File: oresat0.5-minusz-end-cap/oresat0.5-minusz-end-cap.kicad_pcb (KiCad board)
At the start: 2 copper layers, 106 x 106 mm, 36 parts, among them U1 TCA9543A-PW, U3 HMC5883L, U4 HMC5883L

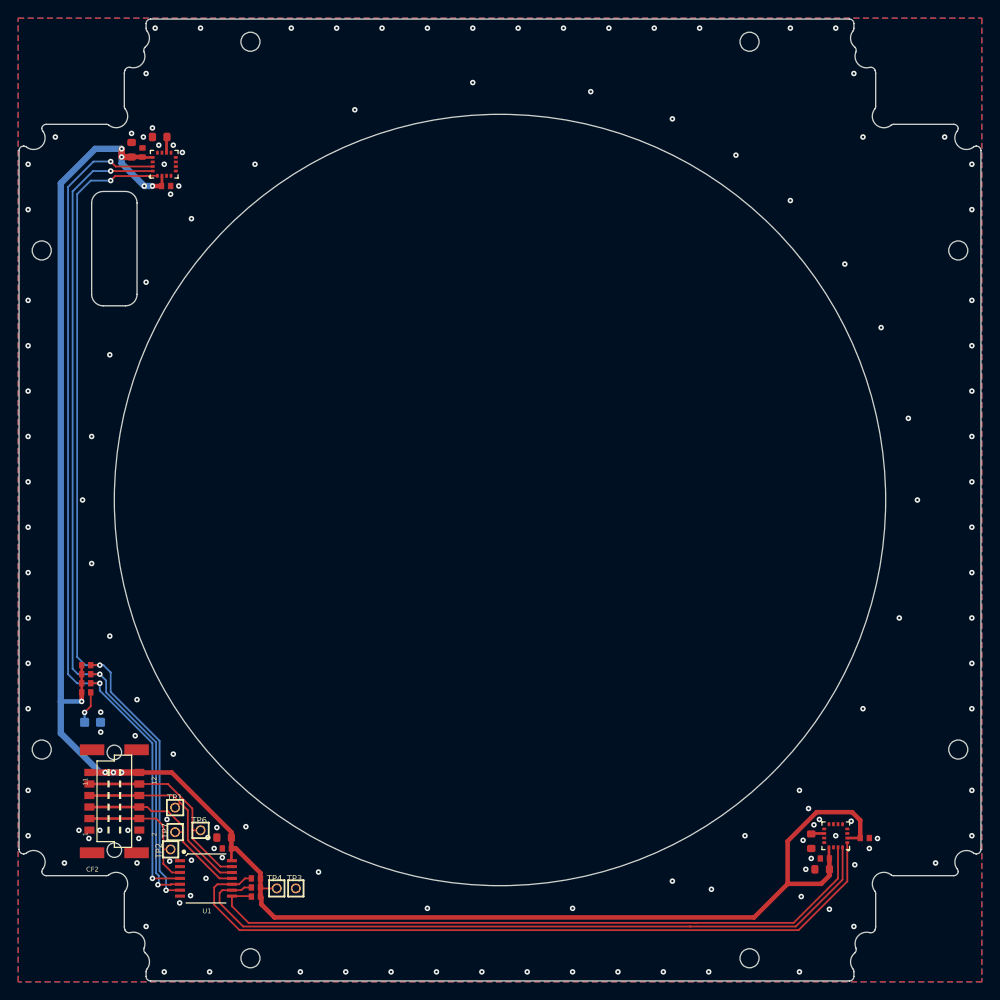
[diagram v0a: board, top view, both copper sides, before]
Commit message: Updated both oresat0.5 end caps. Fixed layout, and added patch antennas
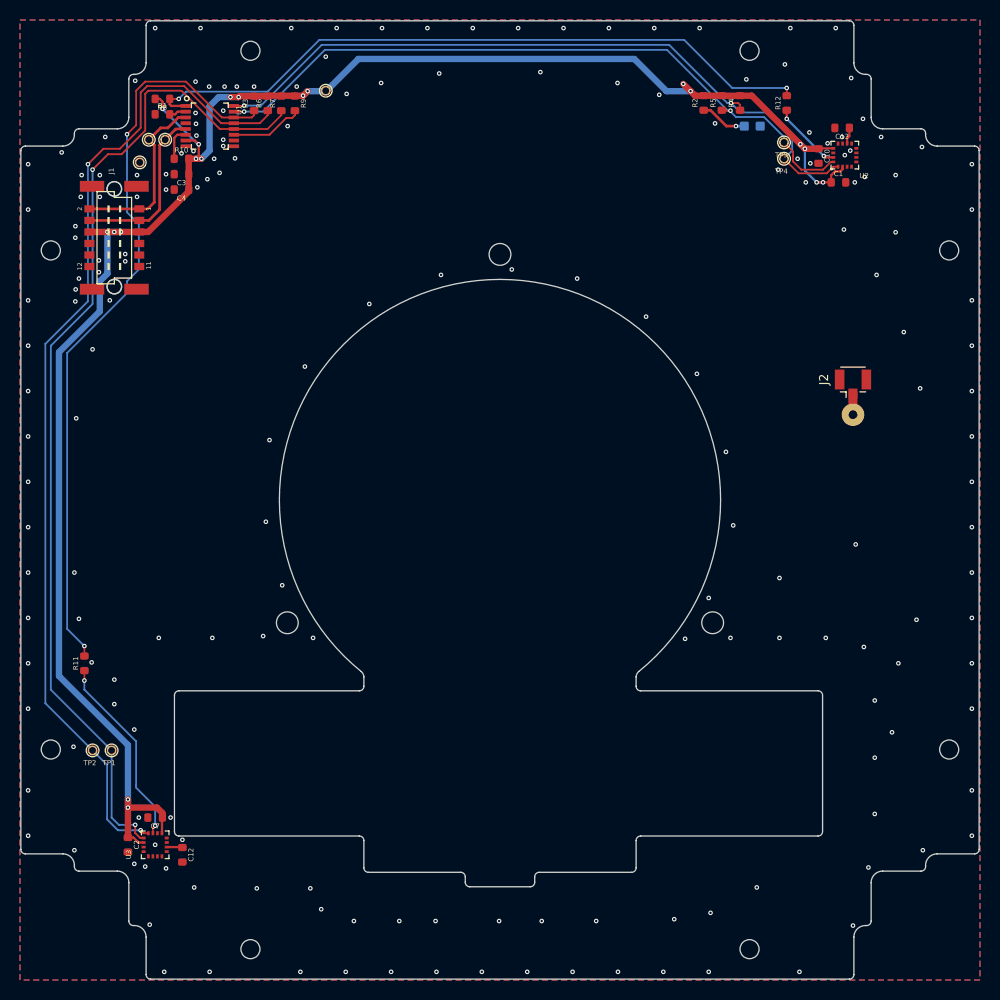
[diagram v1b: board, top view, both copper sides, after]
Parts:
- removed @HOLE0, @HOLE1, @HOLE2, @HOLE3, @HOLE4, @HOLE5, @HOLE6, @HOLE7: , 
- removed C15, C19: 4.7u, minusz-end-cap:.0603-B-NOSILK
- removed CF2: J-HARWIN-M55-70X1242R, minusz-end-cap:HARWIN-M55-70X1242R
- removed U4: HMC5883L, minusz-end-cap:QLGA-16(3X3)
- added ANT1: GP.1575.25.2.A.02, oresat-misc:Taoglas-GPS-Patch-Antenna, B.Cu at (187.4, 93.1)
- added J1: , oresat0.5-minusz-end-cap:HARWIN-M55-70X1242R, F.Cu at (106.0, 76.1)
- added J2: U.FL-R-SMA, Connector_Coaxial:U.FL_Hirose_U.FL-R-SMT-1_Vertical, F.Cu at (187.4, 92.2)
- added R10: , oresat0.5-minusz-end-cap:.0603-B-NOSILK, F.Cu at (113.4, 67.4)
- added R11: NP, oresat0.5-minusz-end-cap:.0603-B-NOSILK, F.Cu at (102.7, 123.0)
- added R12: NP, oresat0.5-minusz-end-cap:.0603-B-NOSILK, F.Cu at (180.1, 61.2)
- added R8: , oresat0.5-minusz-end-cap:.0603-B-NOSILK, F.Cu at (111.3, 60.8)
- added R9: , oresat0.5-minusz-end-cap:.0603-B-NOSILK, F.Cu at (125.9, 61.3)
- added REF**: MountingHole_2.1mm, MountingHole:MountingHole_2.1mm, B.Cu at (198.0, 132.5)
- added REF**: MountingHole_2.1mm, MountingHole:MountingHole_2.1mm, B.Cu at (99.0, 77.5)
- added REF**: MountingHole_2.1mm, MountingHole:MountingHole_2.1mm, B.Cu at (121.0, 154.5)
- added REF**: MountingHole_2.1mm, MountingHole:MountingHole_2.1mm, B.Cu at (198.0, 77.5)
- added REF**: MountingHole_2.1mm, MountingHole:MountingHole_2.1mm, B.Cu at (176.0, 55.5)
- added REF**: MountingHole_2.1mm, MountingHole:MountingHole_2.1mm, B.Cu at (99.0, 132.5)
- added REF**: MountingHole_2.1mm, MountingHole:MountingHole_2.1mm, B.Cu at (176.0, 154.5)
- added REF**: MountingHole_2.1mm, MountingHole:MountingHole_2.1mm, B.Cu at (121.0, 55.5)
- added TP5: TEST-POINT-LARGE-SQUARE, oresat0.5-minusz-end-cap:1X01, B.Cu at (179.8, 65.6)
- added TP8: TEST-POINT-LARGE-SQUARE, oresat0.5-minusz-end-cap:1X01, F.Cu at (108.8, 67.8)
- added U2: , oresat0.5-minusz-end-cap:LGA-16(3X3), F.Cu at (186.5, 67.0)
- C1, C10, C2, C3, C7: value 100n -> (none); footprint minusz-end-cap:.0402-B-NOSILK -> oresat0.5-minusz-end-cap:.0603-B-NOSILK
- C12, C13, C4: value 10u -> (none); footprint minusz-end-cap:.0603-B-NOSILK -> oresat0.5-minusz-end-cap:.0603-B-NOSILK
- D2: value GREEN -> (none); footprint minusz-end-cap:LED-0603 -> oresat0.5-minusz-end-cap:LED-0603
- R1, R3, R4, R5, R6, R7: value 4.7k -> (none); footprint minusz-end-cap:.0402-B-NOSILK -> oresat0.5-minusz-end-cap:.0603-B-NOSILK
- R2: value 2.7k -> (none); footprint minusz-end-cap:.0402-B-NOSILK -> oresat0.5-minusz-end-cap:.0603-B-NOSILK
- TP1, TP2, TP4: value TEST-POINT -> TEST-POINT-LARGE-SQUARE; footprint minusz-end-cap:2MM-TEST-POINT -> oresat0.5-minusz-end-cap:1X01; moved to B.Cu
- TP3, TP6, TP7: value TEST-POINT -> TEST-POINT-LARGE-SQUARE; footprint minusz-end-cap:2MM-TEST-POINT -> oresat0.5-minusz-end-cap:1X01
- U1: value TCA9543A-PW -> (none); footprint minusz-end-cap:TSSOP14-0.65-5.4X4.4MM -> oresat0.5-minusz-end-cap:16-SSOP
- U3: value HMC5883L -> (none); footprint minusz-end-cap:QLGA-16(3X3) -> oresat0.5-minusz-end-cap:LGA-16(3X3)
- moved D2 98.0 mm to (176.3, 63.8)
- moved TP4 97.9 mm to (179.8, 67.4), turned to 180 degrees
- moved R4 95.0 mm to (174.9, 61.2), turned to 90 degrees
- moved R5 94.2 mm to (172.9, 61.2), turned to 90 degrees
- moved R2 94.1 mm to (170.9, 61.2), turned to 90 degrees
- moved R3 87.4 mm to (121.4, 61.3), turned to 90 degrees
- moved R6 86.4 mm to (122.9, 61.3), turned to 90 degrees
- moved R7 85.4 mm to (124.4, 61.3), turned to 90 degrees
- moved TP3 83.8 mm to (111.6, 65.3), turned to -90 degrees
- moved TP7 83.4 mm to (129.3, 59.9), turned to -90 degrees
- moved U1 82.9 mm to (116.5, 63.8)
- moved C2 81.2 mm to (107.5, 143.0), turned to -90 degrees
- moved TP6 76.3 mm to (109.8, 65.3)
- moved C13 75.2 mm to (186.2, 64.0)
- moved U3 75.0 mm to (110.5, 143.0), turned to 90 degrees
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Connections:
- R1 pad 1: ~{INT0} -> GND
- R1 pad 2: 3.3V -> Net-(R1-Pad2)
- R3 pad 1: ~{INT1} -> Net-(R3-Pad1)
- R4 pad 1: SCL0 -> /SCL2
- R5 pad 1: SDA0 -> /SDA2
- R6 pad 1: SD1 -> /SDA1
- R7 pad 1: SC1 -> /SCL1
- TP1 pad 1: I2C-SCL -> /SCL1
- TP2 pad 1: ~{I2C-RESET} -> /SDA1
- TP3 pad 1: GND -> /I2C-SCL
- TP4 pad 1: 3.3V -> /SCL2
- TP6 pad 1: I2C-SDA -> /I2C-SDA
- TP7 pad 1: I2C-~{INT} -> 3.3V
- U1 pad 1: GND -> Net-(R8-Pad1)
- U1 pad 10: SC1 -> GND
- U1 pad 11: I2C-~{INT} -> Net-(R9-Pad2)
- U1 pad 12: I2C-SCL -> /SCL1
- U1 pad 13: I2C-SDA -> /SDA1
- U1 pad 14: 3.3V -> Net-(R3-Pad1)
- U1 pad 2: GND -> Net-(R1-Pad2)
- U1 pad 3: ~{I2C-RESET} -> /I2C-SDA
- U1 pad 4: ~{INT0} -> GND
- U1 pad 5: SDA0 -> /I2C-SCL
- U1 pad 6: SCL0 -> Net-(R10-Pad1)
- U1 pad 7: GND -> 3.3V
- U1 pad 8: ~{INT1} -> GND
- U1 pad 9: SD1 -> GND
- U3 pad 1: SC1 -> /SCL1
- U3 pad 15: ~{INT1} -> Net-(R11-Pad1)
- U3 pad 16: SD1 -> /SDA1
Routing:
- net /SCL1: track 0.00 -> 110.8 mm, vias 0 -> 2
- net /SDA1: track 0.00 -> 110.4 mm, vias 0 -> 2
- net ~{INT0}: track 96.3 -> 0.00 mm, vias 3 -> 0
- net SDA0: track 95.0 -> 0.00 mm, vias 3 -> 0
- net SCL0: track 94.2 -> 0.00 mm, vias 3 -> 0
- net SC1: track 83.9 -> 0.00 mm
- net Net-(R3-Pad1): track 0.00 -> 83.0 mm, vias 0 -> 2
- net SD1: track 80.3 -> 0.00 mm
- net /SCL2: track 0.00 -> 79.8 mm, vias 0 -> 2
- net /SDA2: track 0.00 -> 76.7 mm, vias 0 -> 3
- net ~{INT1}: track 76.3 -> 0.00 mm
- net Net-(R8-Pad1): track 0.00 -> 76.2 mm, vias 0 -> 2
- net I2C-SDA: track 22.3 -> 0.00 mm
- net I2C-SCL: track 21.9 -> 0.00 mm
- net Net-(R11-Pad1): track 0.00 -> 21.3 mm, vias 0 -> 2
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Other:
- board size 106 x 106 mm -> 105.6 x 105.6 mm
- board text added: "2022/02/17"
- board text added: "OreSat0.5 -Z End Cap v1.0"
- board text removed: "OreSat -Z End Cap v1.0"

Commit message: Updated both OreSat0.5 end caps and cleaned up errors
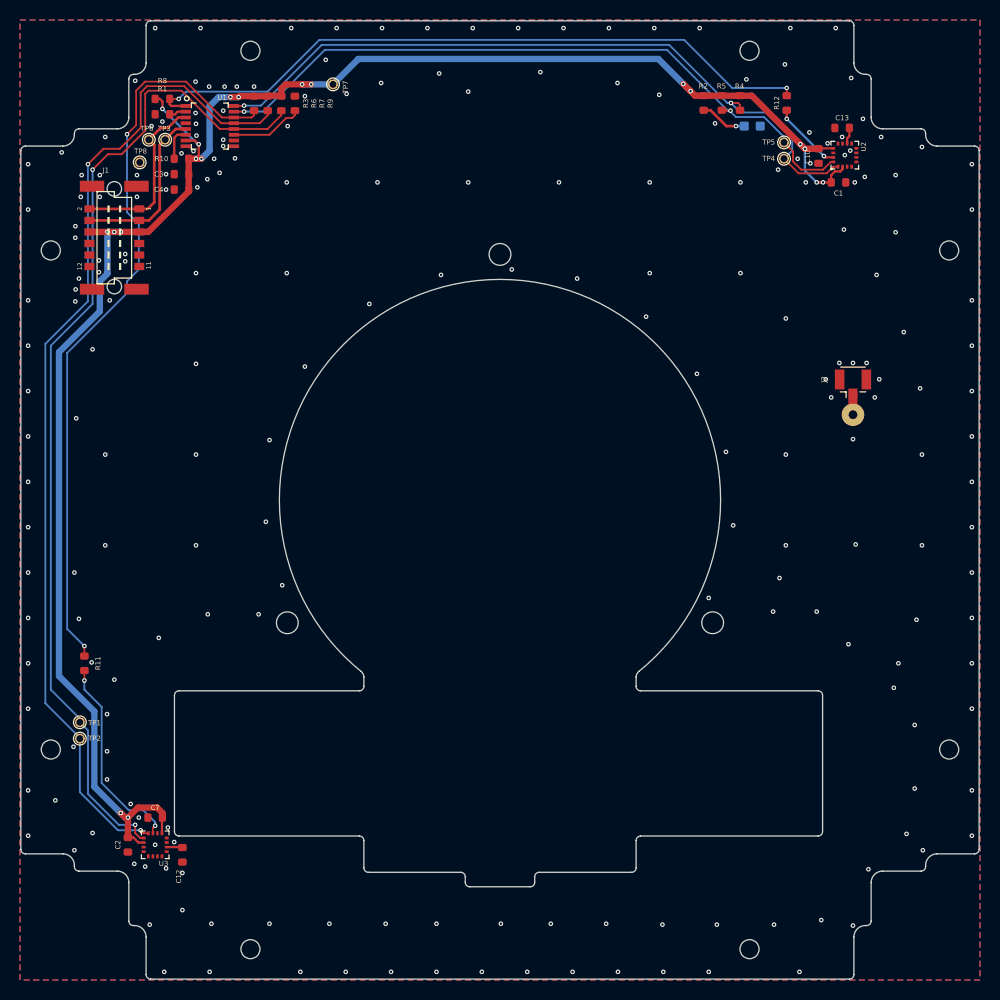
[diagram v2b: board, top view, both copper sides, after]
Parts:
- added REF**: Hole-2.4mm-NPTH, oresat-misc:Hole-2.4mm-NPTH, F.Cu at (125.1, 118.5)
- added REF**: Hole-2.4mm-NPTH, oresat-misc:Hole-2.4mm-NPTH, F.Cu at (171.9, 118.5)
- added REF**: Hole-2.4mm-NPTH, oresat-misc:Hole-2.4mm-NPTH, F.Cu at (148.5, 77.9)
- TP6, TP7, TP8: moved to B.Cu
- moved TP1 4.68 mm to (102.2, 129.5)
- moved TP2 1.91 mm to (102.2, 131.3)
- moved TP7 1.06 mm to (130.1, 59.2)
- turned TP8 to 0 degrees
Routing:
- net 3.3V: track 204.8 -> 207.1 mm
- net Net-(R11-Pad1): track 21.3 -> 22.2 mm
- net GND: track 0.31 -> 0.01 mm, vias 189 -> 224
- net /SDA2: vias 3 -> 2
- net (no net): vias 1 -> 0
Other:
- outline, holes or cut-outs redrawn

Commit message: OreSat0.5 end caps design review fixes
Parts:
- U2, U3: value (none) -> MMC5883MA
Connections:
- net /I2C-SCL renamed /MAG-SCL
- net /I2C-SDA renamed /MAG-SDA
- U1 pad 10: GND -> unconnected-(U1-Pad10)
- U1 pad 8: GND -> unconnected-(U1-Pad8)
- U1 pad 9: GND -> unconnected-(U1-Pad9)
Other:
- board text added: "2022/02/19"
- board text removed: "2022/02/17"
